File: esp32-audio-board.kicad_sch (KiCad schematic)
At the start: 123 parts, among them IC1 XC6220A331MR-G, IC2 XC6220A331MR-G, J1 EN_PAD0, J10 PWR_LED+, J11 HP_LOUT1, J12 HP_ROUT1, J13 HP_LOUT2, J14 HP_ROUT2, J15 MIC_LIN1, J16 MIC_LIN1_GND, J17 MIC_RIN1, J18 MIC_RIN1_GND, J19 HP_1GND, J2 Conn_01x02_Pin, J20 HP_2GND, J21 VP_PAD0, J22 PWR_LED-, J23 CHG_LED+, J24 CHG_LED-, J3 USB_C_Receptacle_USB2.0_16P, J4 EN_PAD1, J5 VP_PAD1, J6 VN_PAD0, J7 VN_PAD1, J8 IO34_PAD0, J9 IO34_PAD1, Q1 SS8050, Q2 SS8050, Q4 AO3401A, U1 ESP32-WROOM-32E, U2 CH340C, U3 MCP73831-2-OT, U5 ES8388

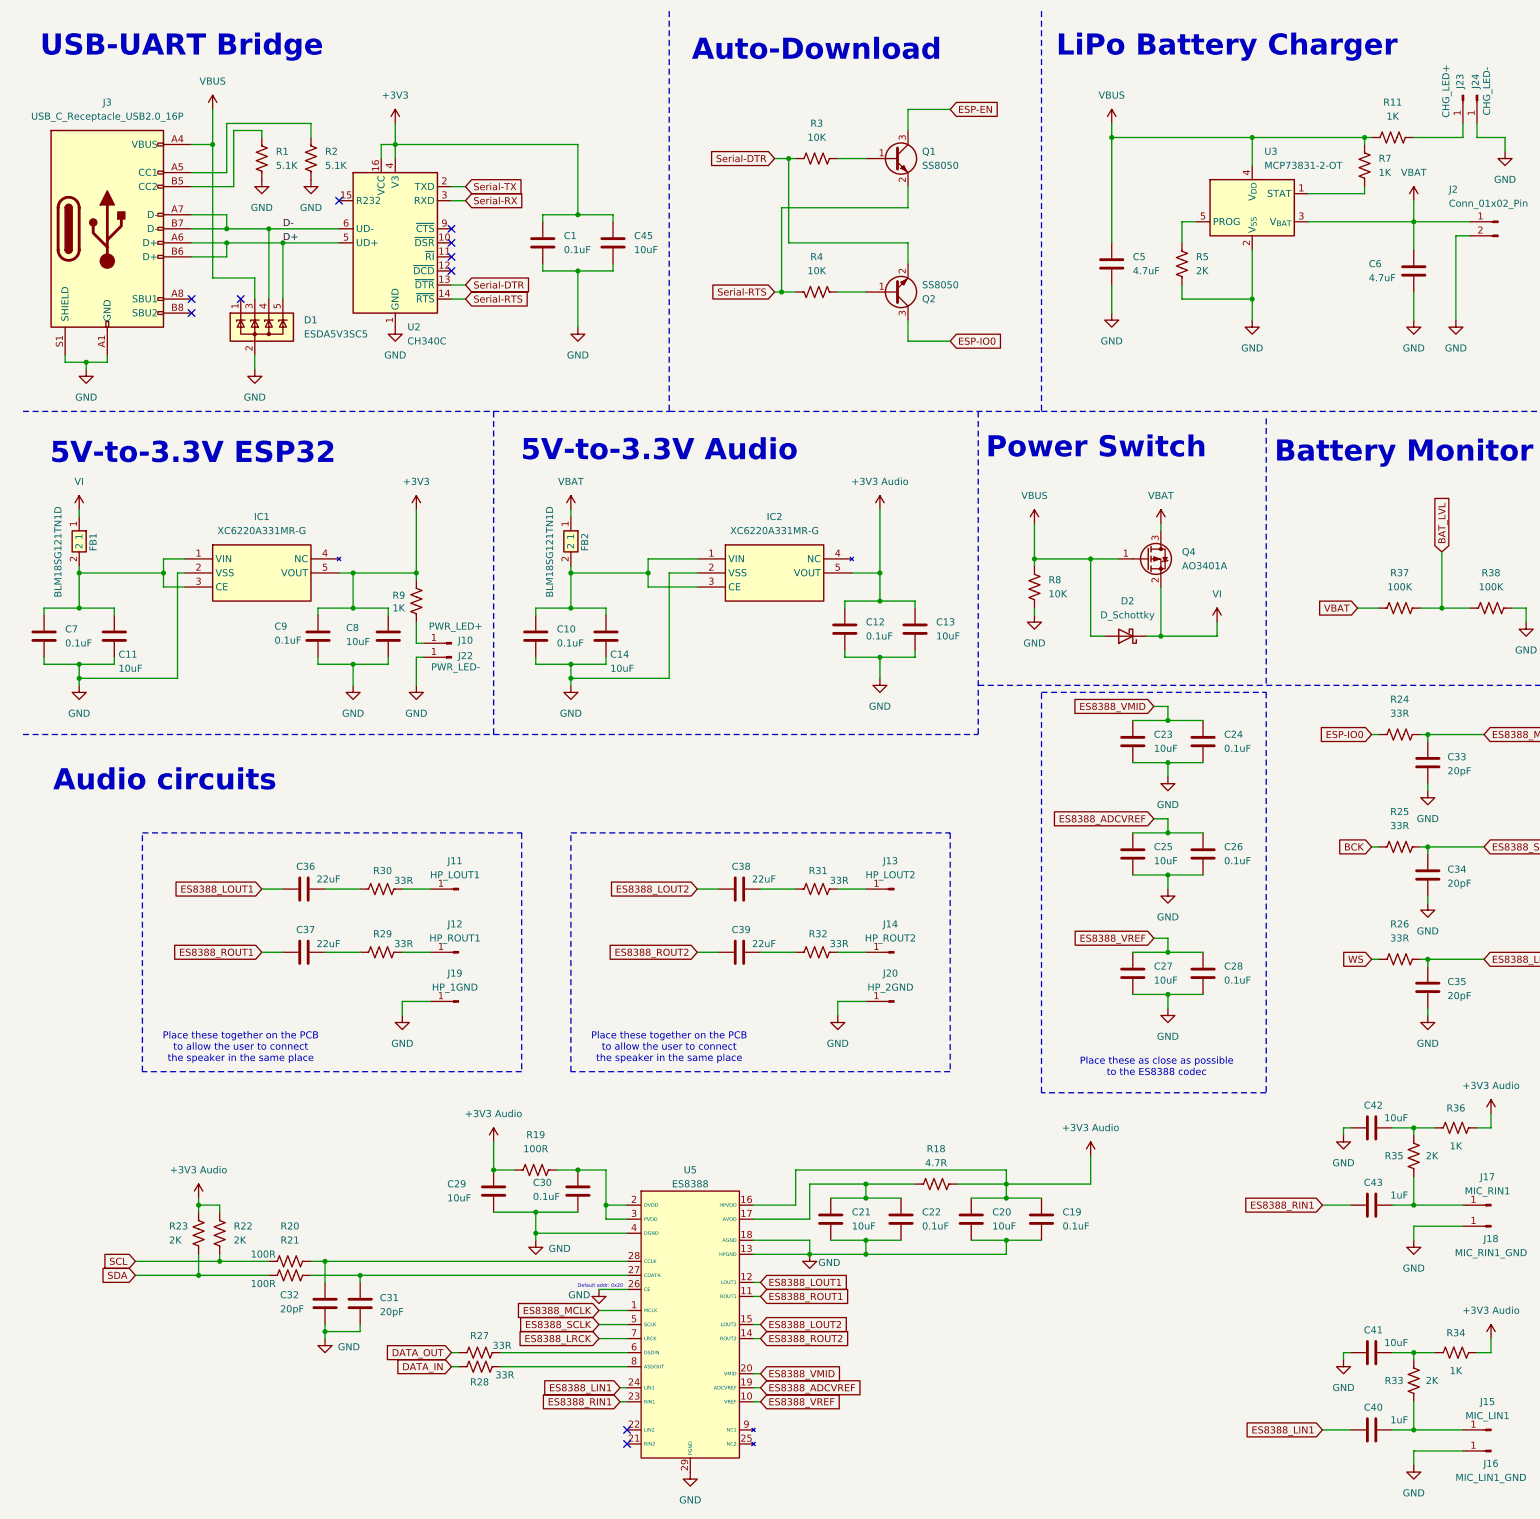
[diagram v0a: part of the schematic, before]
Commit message: esp32-audio-board: complete PCB general design
Added the initial PCB complete design.

Changed the CH340C with CP2102 to allow the board to
consume less energy while not connected to USB.

Signed-off-by: RaresCon <rares.constantin2002@gmail.com>
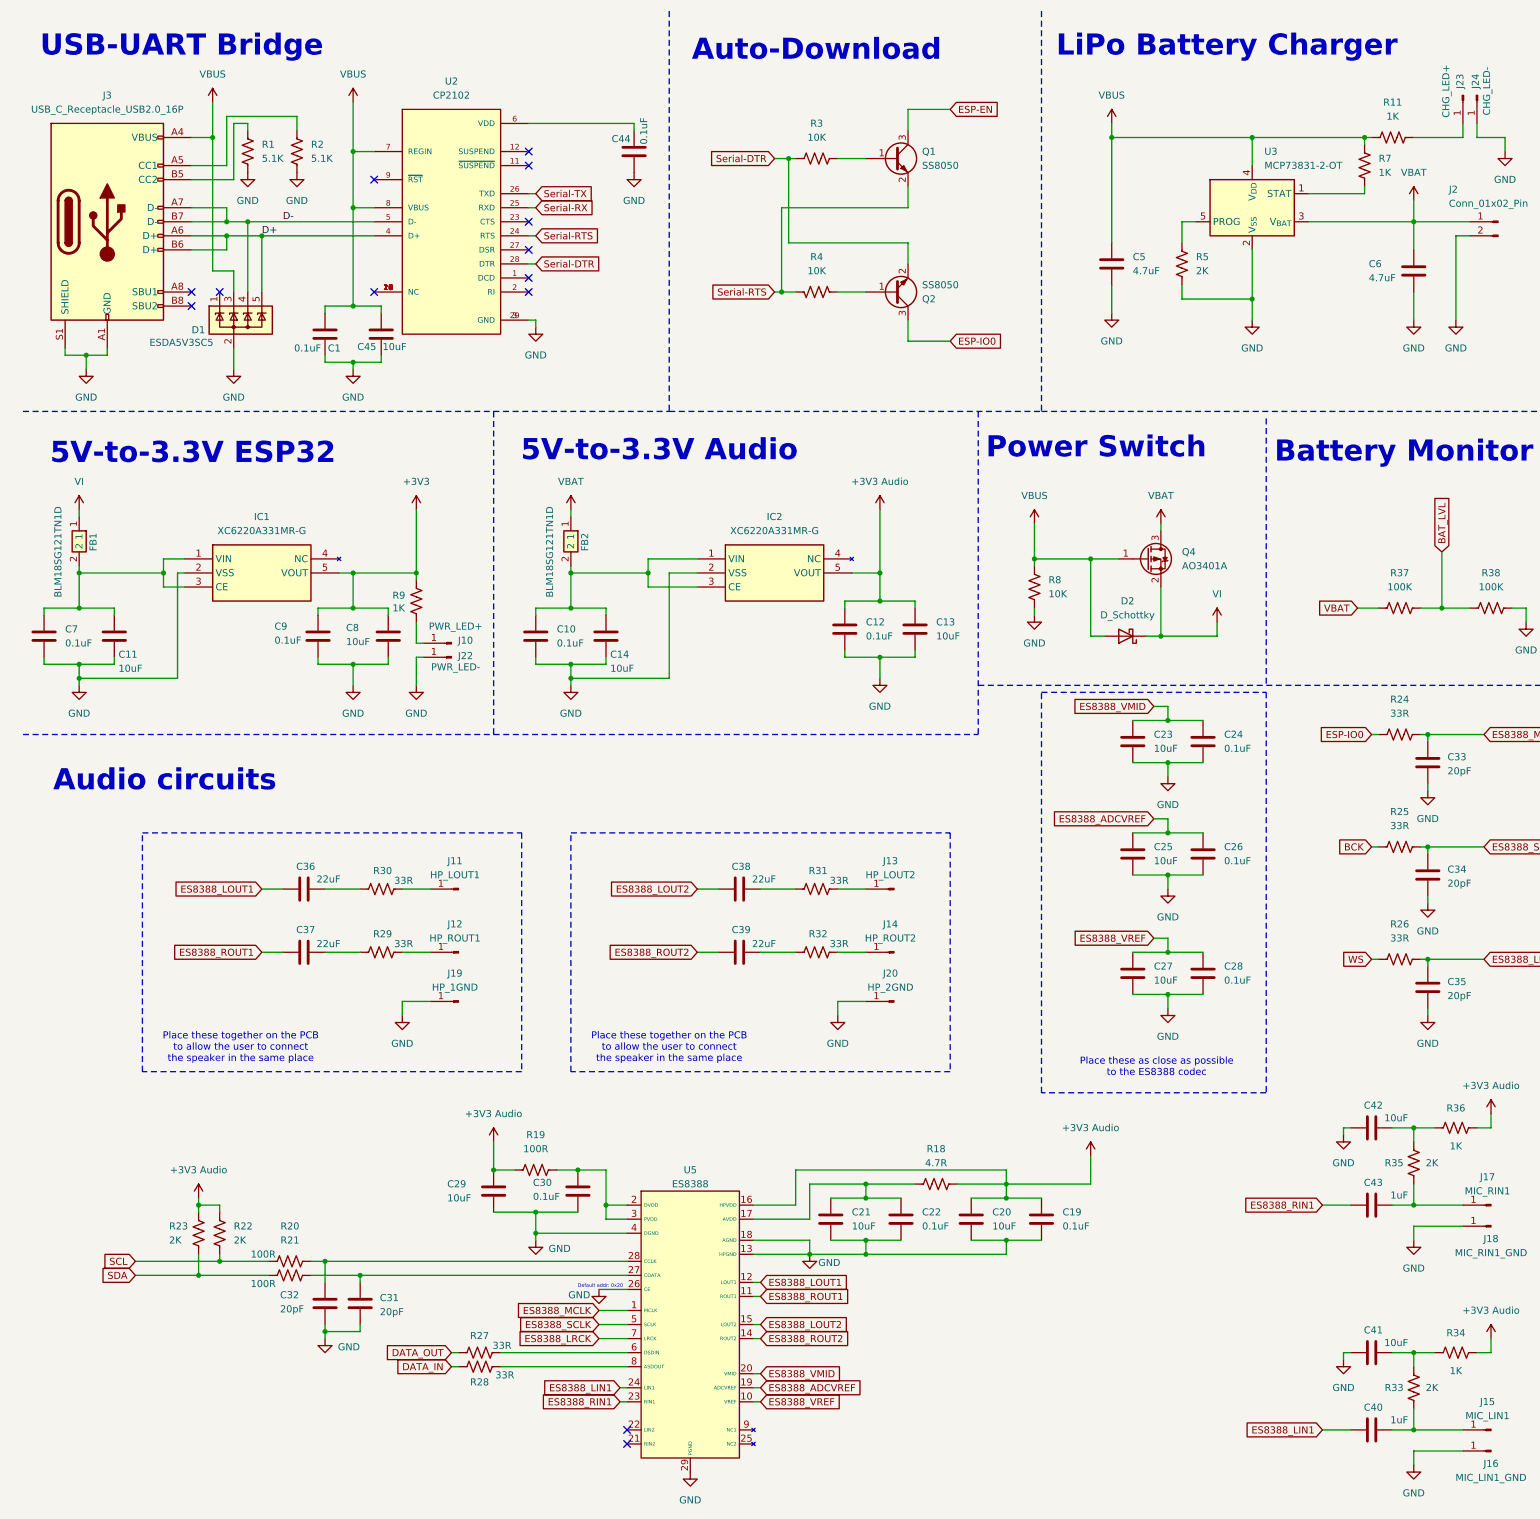
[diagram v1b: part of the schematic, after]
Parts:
- removed U2: CH340C, Package_SO:SOIC-16_3.9x9.9mm_P1.27mm, symbol Interface_USB:CH340C
- added C44: 0.1uF, Capacitor_SMD:C_0402_1005Metric_Pad0.74x0.62mm_HandSolder, symbol Device:C
- added U2: CP2102, cp2102:QFN50P500X500X100-29N, symbol CP2102:CP2102
- FB1, FB2: footprint BLM18EG101TH1D -> blm18sg121tn1d:BLM18EG101TH1D
- U1: footprint RF_Module:ESP32-WROOM-32D -> RF_Module:ESP32-WROOM-32E
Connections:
- net +3V3: no longer C1.1, C45.1
- net D+: now also U2.4 (D+)
- net D-: now also U2.5 (D-)
- net GND: now also C44.2, U2.29 (GND), U2.3 (GND)
- net Serial-DTR: now also U2.28 (DTR)
- net Serial-RTS: now also U2.24 (RTS)
- net Serial-RX: now also U2.25 (RXD)
- net Serial-TX: now also U2.26 (TXD)
- net VBUS: now also C1.1, C45.1, U2.7 (REGIN), U2.8 (VBUS)
- new net: U2.10 (NC), U2.13 (NC), U2.14 (NC), U2.15 (NC), U2.16 (NC), U2.17 (NC), U2.18 (NC), U2.19 (NC), U2.20 (NC), U2.21 (NC), U2.22 (NC)
- new net: C44.1, U2.6 (VDD)
- no-connect marks 22 -> 25
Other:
- moved on the sheet: C1, C45, D1, J3, R1, R2, R33, R35

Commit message: esp32-audio-board: complete PCB
Added all the pads and connections for external input
and output. Made the board smaller to allow the case
to be slimmer.

Signed-off-by: RaresCon <rares.constantin2002@gmail.com>
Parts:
- D2: value D_Schottky -> 3A/20V/390mV - SBR3U20SA-13; footprint Diode_SMD:D_3220_8050Metric_Pad2.65x5.15mm_HandSolder -> Diode_SMD:D_SMA
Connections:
- net BAT_LVL renamed ESP_IO35
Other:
- note added: "Play/Pause/Deepsleep"
- note removed: "Play/Pause"

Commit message: esp32-audio-board: PCB improvements
Rerouted the buttons pins to not use the SENSOR_VN
and SENSOR_VP pins, avoiding any problems with not
being able to pull-up/down them. Added all the
silkscreen texts and reduced the DRC warnings to 1
(silkscreen overlap).

Signed-off-by: RaresCon <rares.constantin2002@gmail.com>
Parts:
- C1, C10, C12, C15, C16, C17, C18, C19, C22, C3, C30, C44, C7, C9: value 0.1uF -> 0.1uF/1%
- C11, C13, C14, C20, C21, C29, C41, C42, C45, C8: value 10uF -> 10uF/1%
- C2, C36, C37, C38, C39: value 22uF -> 22uF/1%
- C31, C32, C33, C34, C35: value 20pF -> 20pF/1%
- C40, C43: value 1uF -> 1uF/1%
- C5, C6: value 4.7uF -> 4.7uF/1%
- C_EN1: renamed from C4; value 0.1uF -> 0.1uF/1%
- D2: value 3A/20V/390mV - SBR3U20SA-13 -> 3A/20V Schottky Rectifier - MBRA320
- J2: value Conn_01x02_Pin -> JST S2B
- R1: value 5.1K -> 5.1K/1%
- R10: value 10K -> 10K/1%
- R11, R34, R36, R9: value 1K -> 1K/1%
- R13, R14, R16, R19, R20, R21: value 100R -> 100R/1%
- R18: value 4.7R -> 4.7R/1%
- R2: value 5.1K -> 5.1K/%1
- R24, R25, R26, R27, R28, R29, R30, R31, R32: value 33R -> 33R/1%
- R33, R35: value 2K -> 2K/1%
- R7: value 1K -> 1K/%1
- R_EN1: renamed from R6; value 10K -> 10K/1%
- R_PROG1: renamed from R5; value 2K -> 2K/1%
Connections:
- net ESP_IO25: now reaches U1.10 (IO25)
- net ESP_IO25: now also R16.1, R17.1
- net ESP_IO32: now reaches U1.8 (IO32)
- net ESP_IO32: now also R12.1, R13.1
- net ESP_IO33: now reaches U1.9 (IO33)
- net ESP_IO33: now also R14.1, R15.1
- removed net ESP_IO34: R16.1, R17.1, U1.6 (IO34)
- removed net ESP_SENSOR_VN: R14.1, R15.1, U1.5 (SENSOR_VN)
- removed net ESP_SENSOR_VP: R12.1, R13.1, U1.4 (SENSOR_VP)
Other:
- moved on the sheet: C6

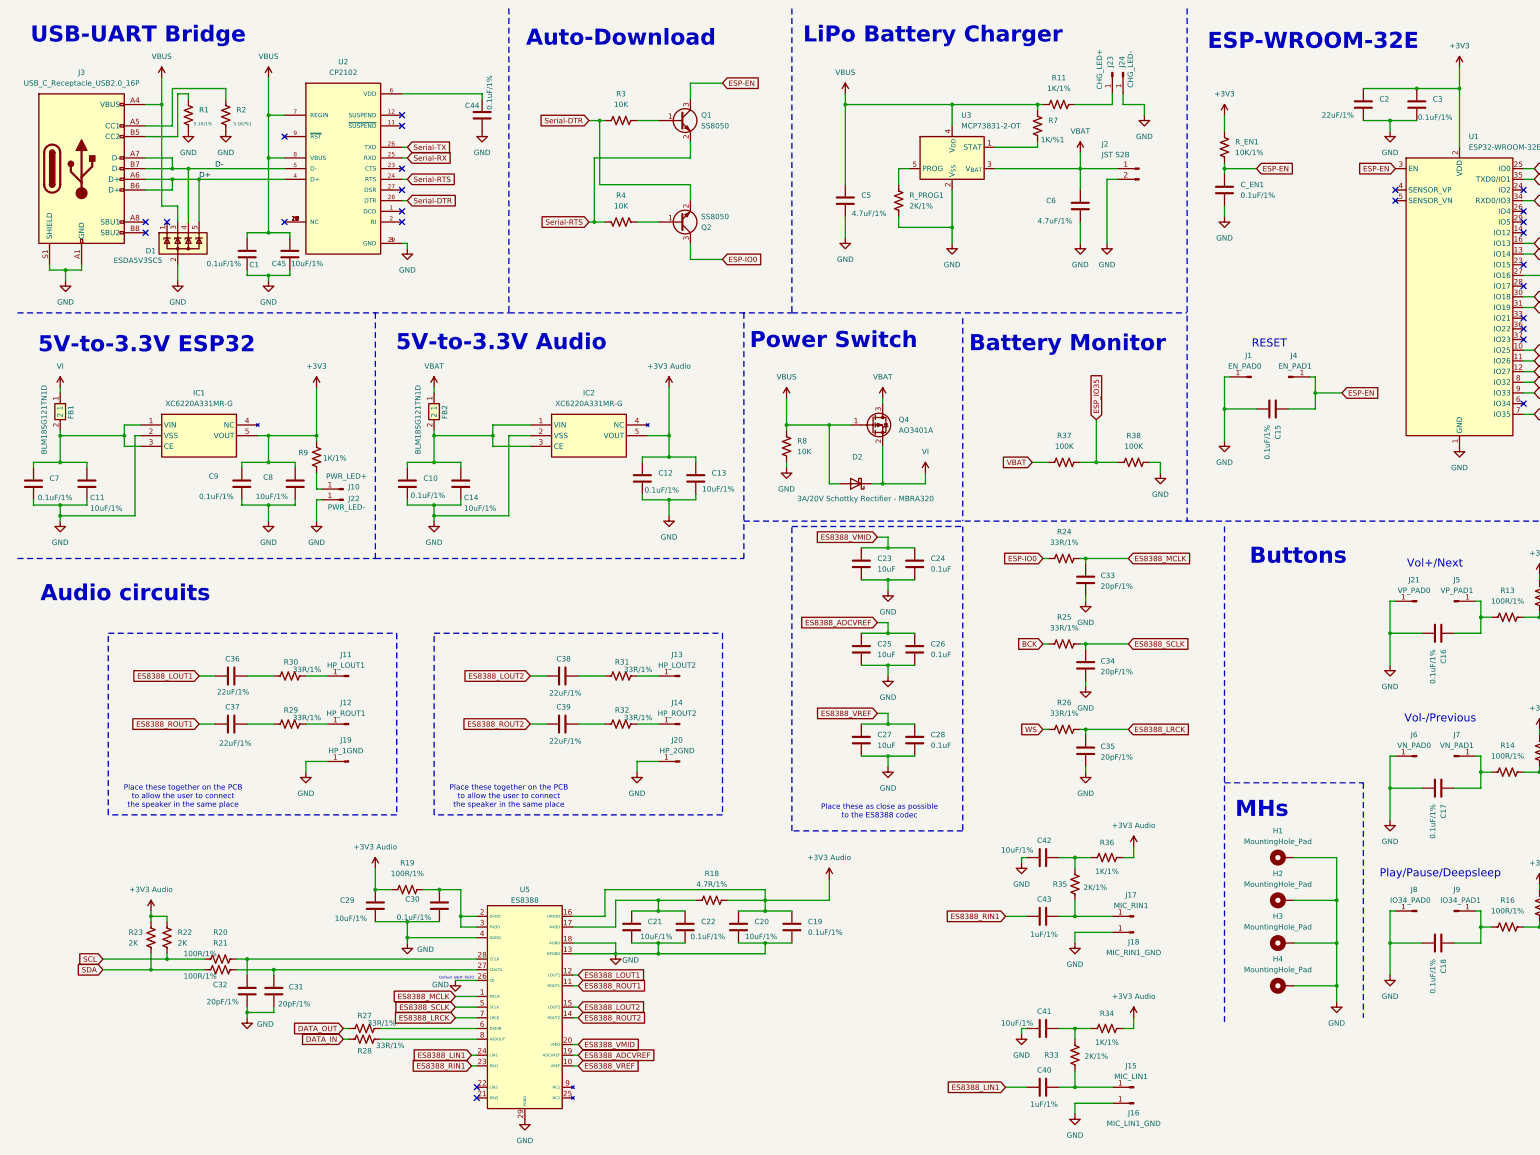
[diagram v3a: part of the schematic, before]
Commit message: esp32-audio-board: power changes
Changed the LDOs to make the PCB more power
efficient and try to find these parts in stock.
Changed the footprint for the Q4 to be more compact.

Signed-off-by: RaresCon <rares.constantin2002@gmail.com>
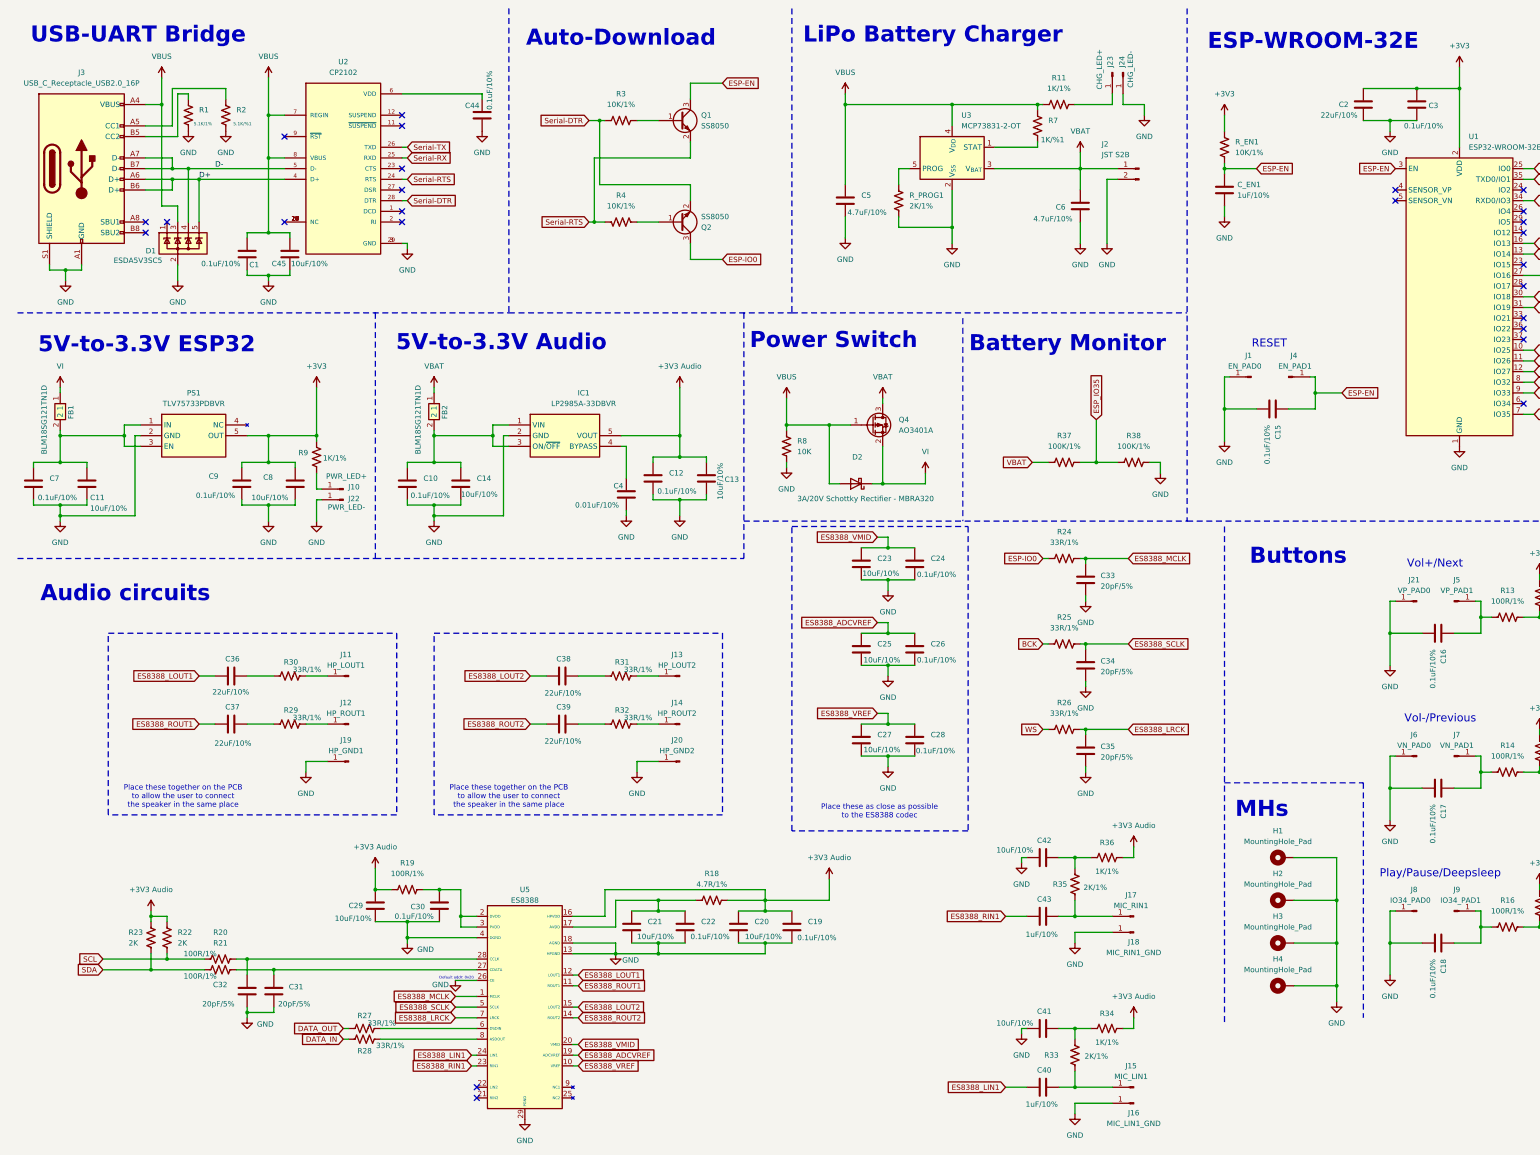
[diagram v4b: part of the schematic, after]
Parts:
- removed IC1, IC2: XC6220A331MR-G, xc6220a331:SOT95P280X120-5N, symbol XC6220A331MR-G:XC6220A331MR-G
- added C4: 0.01uF/10%, Capacitor_SMD:C_0402_1005Metric_Pad0.74x0.62mm_HandSolder, symbol Device:C
- added IC1: LP2985A-33DBVR, lp2985a-33dbvr:SOT95P280X145-5N, symbol LP2985A-33DBVR:LP2985A-33DBVR
- added PS1: TLV75733PDBVR, tlv75733pdbvr:SOT95P280X145-5N, symbol TLV75733PDBVR:TLV75733PDBVR
- C1, C10, C12, C15, C16, C17, C18, C19, C22, C3, C30, C44, C7, C9: value 0.1uF/1% -> 0.1uF/10%
- C11, C13, C14, C20, C21, C29, C41, C42, C45, C8: value 10uF/1% -> 10uF/10%
- C2, C36, C37, C38, C39: value 22uF/1% -> 22uF/10%
- C23, C25, C27: value 10uF -> 10uF/10%
- C24, C26, C28: value 0.1uF -> 0.1uF/10%
- C31, C32, C33, C34, C35: value 20pF/1% -> 20pF/5%
- C40, C43: value 1uF/1% -> 1uF/10%
- C5, C6: value 4.7uF/1% -> 4.7uF/10%
- C_EN1: value 0.1uF/1% -> 1uF/10%
- J19: value HP_1GND -> HP_GND1
- J20: value HP_2GND -> HP_GND2
- Q4: footprint Package_TO_SOT_SMD:SOT-23_Handsoldering -> Package_TO_SOT_SMD:SOT-23
- R3, R4: value 10K -> 10K/1%
- R37, R38: value 100K -> 100K/1%
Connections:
- net +3V3: now also PS1.5 (OUT)
- net +3V3 Audio: now also IC1.5 (VOUT)
- net GND: now also C4.2, IC1.2 (GND), PS1.2 (GND)
- net at C10.1, C14.1, FB2.2: now also IC1.1 (VIN), IC1.3 (ON/~{OFF})
- net at C11.1, C7.1, FB1.2: now also PS1.1 (IN), PS1.3 (EN)
- new net: C4.1, IC1.4 (BYPASS)
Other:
- moved on the sheet: C12, C13
